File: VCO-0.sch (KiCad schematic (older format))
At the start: 25 parts, among them SW1 SW_Push, SW2 SW_Push, U1 RC1602A, U2 AS3320

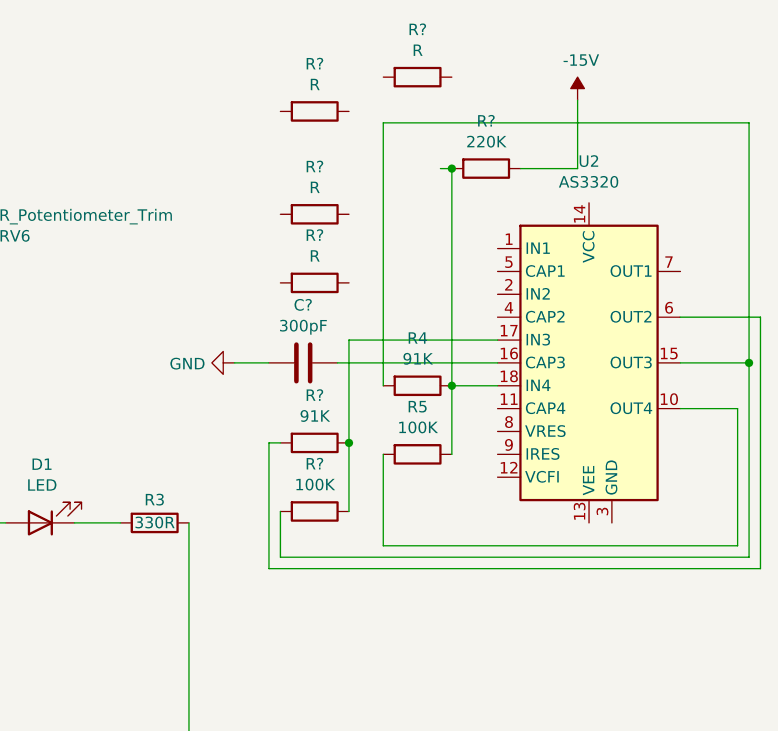
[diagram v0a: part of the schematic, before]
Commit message: Add AS3320 schematic.
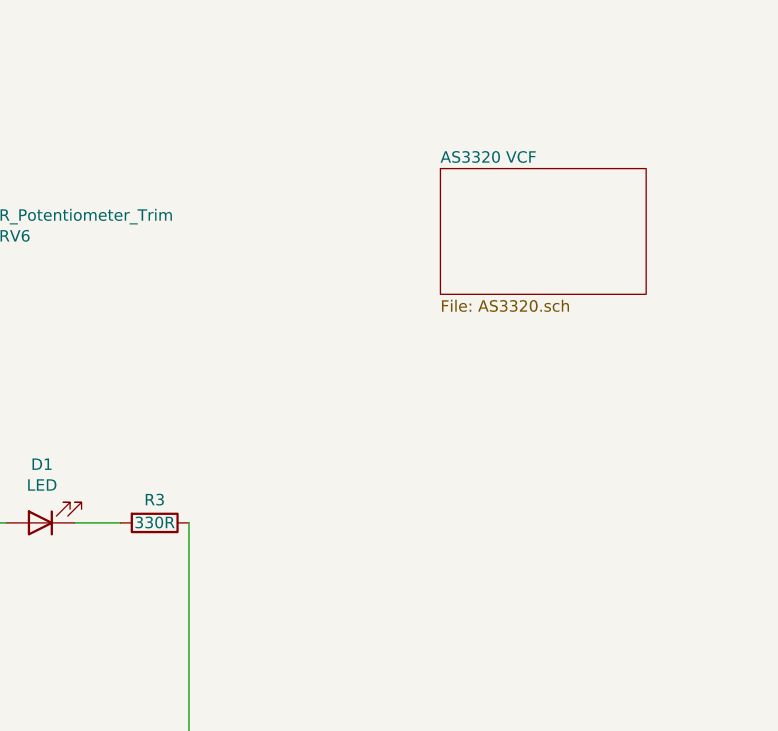
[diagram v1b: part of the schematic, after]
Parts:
- removed C?: 300pF, symbol Device:C
- removed R4, R?: 91K, symbol Device:R
- removed R5, R?: 100K, symbol Device:R
- removed R?: 220K, symbol Device:R
- removed R? (x4): R, symbol Device:R
- removed U2: AS3320, Package_DIP:DIP-18_W7.62mm, symbol Audio:AS3320
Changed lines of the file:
@@
 $Descr A4 11693 8268
 encoding utf-8
-Sheet 1 1
+Sheet 1 2
 Title "VCO-0"
 Date "2020-09-21"
@@
 Wire Wire Line
 	5250 2200 4900 2200
-$Comp
-L Audio:AS3320 U2
-U 1 1 5F6C2199
-P 9450 1900
-F 0 "U2" H 9450 2781 50  0000 C CNN
-F 1 "AS3320" H 9450 2690 50  0000 C CNN
-F 2 "Package_DIP:DIP-18_W7.62mm" H 10050 1600 50  0001 C CNN
-F 3 "http://www.alfarzpp.lv/eng/sc/AS3320.pdf" H 10450 1500 50  0001 C CNN
-	1    9450 1900
-	1    0    0    -1
-$EndComp
-$Comp
-L Device:R R4
-U 1 1 5F6C45EA
-P 8700 2000
-F 0 "R4" V 8493 2000 50  0000 C CNN
-F 1 "91K" V 8584 2000 50  0000 C CNN
-F 2 "" V 8630 2000 50  0001 C CNN
-F 3 "~" H 8700 2000 50  0001 C CNN
-	1    8700 2000
-	0    1    1    0
-$EndComp
-$Comp
-L Device:R R5
-U 1 1 5F6C4F0D
-P 8700 2300
-F 0 "R5" V 8493 2300 50  0000 C CNN
-F 1 "100K" V 8584 2300 50  0000 C CNN
-F 2 "" V 8630 2300 50  0001 C CNN
-F 3 "~" H 8700 2300 50  0001 C CNN
-	1    8700 2300
-	0    1    1    0
-$EndComp
-Wire Wire Line
-	9050 2000 8850 2000
-Wire Wire Line
-	8850 2300 8850 2000
-Connection ~ 8850 2000
-Wire Wire Line
-	8550 850  10150 850
-Wire Wire Line
-	10150 850  10150 1900
-Wire Wire Line
-	10150 1900 9850 1900
-Wire Wire Line
-	8550 2300 8550 2700
-Wire Wire Line
-	8550 2700 10100 2700
-Wire Wire Line
-	10100 2700 10100 2100
-Wire Wire Line
-	10100 2100 9850 2100
-$Comp
-L Device:R R?
-U 1 1 5F6D8851
-P 9000 1050
-F 0 "R?" V 8793 1050 50  0000 C CNN
-F 1 "220K" V 8884 1050 50  0000 C CNN
-F 2 "" V 8930 1050 50  0001 C CNN
-F 3 "~" H 9000 1050 50  0001 C CNN
-	1    9000 1050
-	0    1    1    0
-$EndComp
-Wire Wire Line
-	8850 1050 8800 1050
-Connection ~ 8850 1050
-$Comp
-L power:-15V #PWR?
-U 1 1 5F6DF5E7
-P 9400 750
-F 0 "#PWR?" H 9400 850 50  0001 C CNN
-F 1 "-15V" H 9415 923 50  0000 C CNN
-F 2 "" H 9400 750 50  0001 C CNN
-F 3 "" H 9400 750 50  0001 C CNN
-	1    9400 750
-	1    0    0    -1
-$EndComp
-Wire Wire Line
-	9150 1050 9400 1050
-Wire Wire Line
-	9400 1050 9400 750
-$Comp
-L Device:C C?
-U 1 1 5F6E3993
-P 8200 1900
-F 0 "C?" V 7948 1900 50  0000 C CNN
-F 1 "300pF" V 8039 1900 50  0000 C CNN
-F 2 "" H 8238 1750 50  0001 C CNN
-F 3 "~" H 8200 1900 50  0001 C CNN
-	1    8200 1900
-	0    1    1    0
-$EndComp
-Wire Wire Line
-	8350 1900 9050 1900
-$Comp
-L power:GND #PWR?
-U 1 1 5F6EBD51
-P 7900 1900
-F 0 "#PWR?" H 7900 1650 50  0001 C CNN
-F 1 "GND" V 7905 1772 50  0000 R CNN
-F 2 "" H 7900 1900 50  0001 C CNN
-F 3 "" H 7900 1900 50  0001 C CNN
-	1    7900 1900
-	0    1    1    0
-$EndComp
-Wire Wire Line
-	7900 1900 8050 1900
-$Comp
-L Device:R R?
-U 1 1 5F6F00C9
-P 8250 800
-F 0 "R?" V 8043 800 50  0000 C CNN
-F 1 "R" V 8134 800 50  0000 C CNN
-F 2 "" V 8180 800 50  0001 C CNN
-F 3 "~" H 8250 800 50  0001 C CNN
-	1    8250 800
-	0    1    1    0
-$EndComp
-$Comp
-L Device:R R?
-U 1 1 5F6F0A9B
-P 8700 650
-F 0 "R?" V 8493 650 50  0000 C CNN
-F 1 "R" V 8584 650 50  0000 C CNN
-F 2 "" V 8630 650 50  0001 C CNN
-F 3 "~" H 8700 650 50  0001 C CNN
-	1    8700 650
-	0    1    1    0
-$EndComp
-$Comp
-L Device:R R?
-U 1 1 5F6F1395
-P 8250 1250
-F 0 "R?" V 8043 1250 50  0000 C CNN
-F 1 "R" V 8134 1250 50  0000 C CNN
-F 2 "" V 8180 1250 50  0001 C CNN
-F 3 "~" H 8250 1250 50  0001 C CNN
-	1    8250 1250
-	0    1    1    0
-$EndComp
-$Comp
-L Device:R R?
-U 1 1 5F6F1879
-P 8250 1550
-F 0 "R?" V 8043 1550 50  0000 C CNN
-F 1 "R" V 8134 1550 50  0000 C CNN
-F 2 "" V 8180 1550 50  0001 C CNN
-F 3 "~" H 8250 1550 50  0001 C CNN
-	1    8250 1550
-	0    1    1    0
-$EndComp
-$Comp
-L Device:R R?
-U 1 1 5F6F1C51
-P 8250 2250
-F 0 "R?" V 8043 2250 50  0000 C CNN
-F 1 "91K" V 8134 2250 50  0000 C CNN
-F 2 "" V 8180 2250 50  0001 C CNN
-F 3 "~" H 8250 2250 50  0001 C CNN
-	1    8250 2250
-	0    1    1    0
-$EndComp
-$Comp
-L Device:R R?
-U 1 1 5F6F21E6
-P 8250 2550
-F 0 "R?" V 8043 2550 50  0000 C CNN
-F 1 "100K" V 8134 2550 50  0000 C CNN
-F 2 "" V 8180 2550 50  0001 C CNN
-F 3 "~" H 8250 2550 50  0001 C CNN
-	1    8250 2550
-	0    1    1    0
-$EndComp
-Wire Wire Line
-	8550 850  8550 2000
-Wire Wire Line
-	8850 1050 8850 2000
-Wire Wire Line
-	9050 1800 8400 1800
-Wire Wire Line
-	8400 2550 8400 2250
-Connection ~ 8400 2250
-Wire Wire Line
-	8400 1800 8400 2250
-Wire Wire Line
-	8100 2550 8100 2750
-Wire Wire Line
-	8100 2750 10150 2750
-Wire Wire Line
-	10150 2750 10150 1900
-Connection ~ 10150 1900
-Wire Wire Line
-	8100 2250 8050 2250
-Wire Wire Line
-	8050 2250 8050 2800
-Wire Wire Line
-	8050 2800 10200 2800
-Wire Wire Line
-	10200 2800 10200 1700
-Wire Wire Line
-	10200 1700 9850 1700
+$Sheet
+S 8800 1050 900  550
+U 5F75BB76
+F0 "AS3320 VCF" 50
+F1 "AS3320.sch" 50
+$EndSheet
 $EndSCHEMATC

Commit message: Refactor
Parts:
- RV6: footprint (none) -> Potentiometer_THT:Potentiometer_ACP_CA9-V10_Vertical
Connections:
- no-connect marks 0 -> 1
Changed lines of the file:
@@
 F 0 "RV6" H 6731 1346 50  0000 R CNN
 F 1 "R_Potentiometer_Trim" H 6731 1255 50  0000 R CNN
-F 2 "" H 6800 1300 50  0001 C CNN
+F 2 "Potentiometer_THT:Potentiometer_ACP_CA9-V10_Vertical" H 6800 1300 50  0001 C CNN
 F 3 "~" H 6800 1300 50  0001 C CNN
 	1    6800 1300
@@
 F1 "AS3320.sch" 50
 $EndSheet
+NoConn ~ -3300 -950
 $EndSCHEMATC
